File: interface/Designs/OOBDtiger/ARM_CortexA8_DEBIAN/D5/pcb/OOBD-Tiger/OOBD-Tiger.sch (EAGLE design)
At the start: 88 parts, among them IC3 DS1307, IC4 DS3231, Q2 32.768kHz, U1 SY6280, U10 MP1482DS, U2 SN65HVD230(SO8), U6 SN65HVD230(SO8)

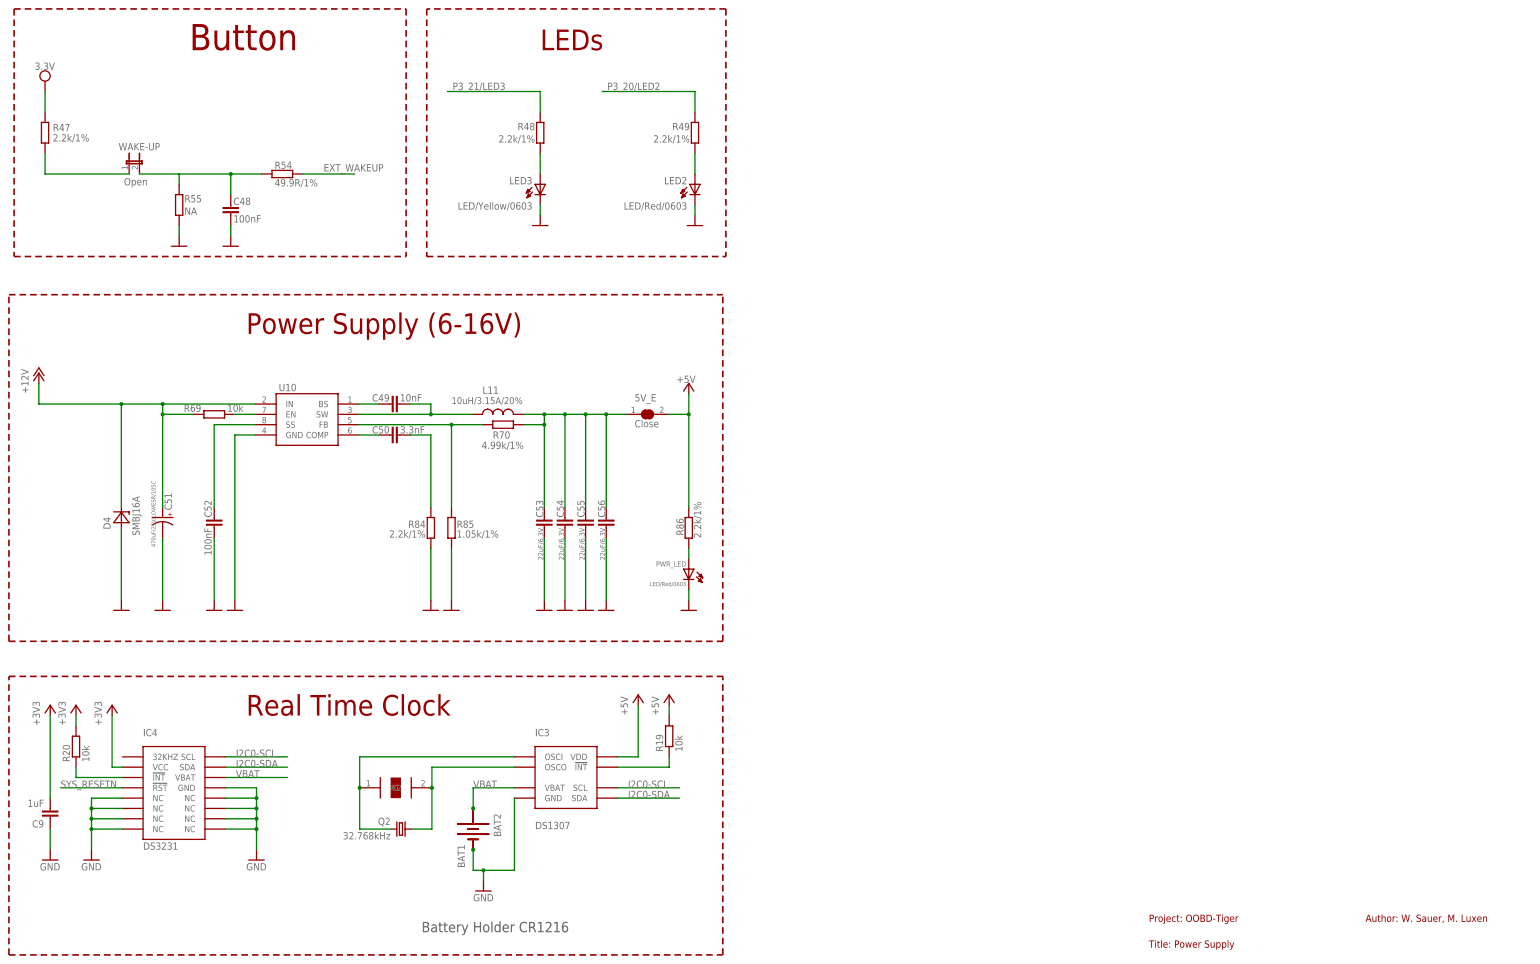
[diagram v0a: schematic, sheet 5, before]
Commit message: - delete further unneeded files(.lbr) - fix and rename Olimex_Connector.lbr to OOBDtiger-Connector.lbr - fix inconsistency error between schematic and pcb - create regular Projects for AM3352-SOM-EVB and OOBD-Tiger.brd - fix all ERC errors (only some uncritical warnings are open) - update OOBD-Tiger.pdf to visualize current status - fix TLV320AIC3107.lbr (=> but sym and dev is missing)
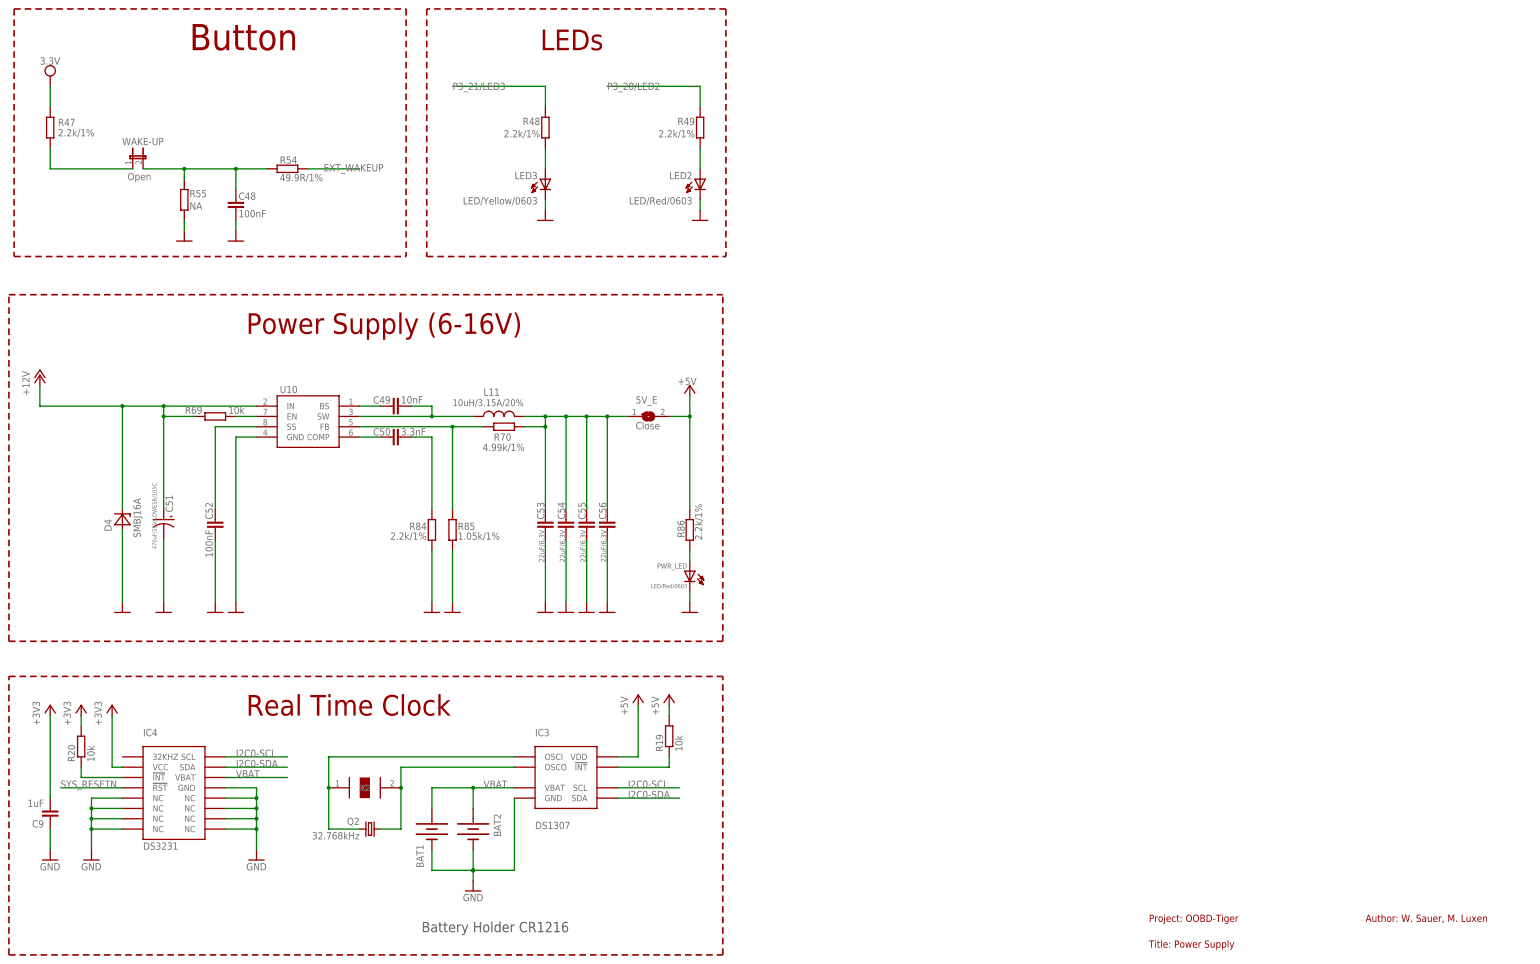
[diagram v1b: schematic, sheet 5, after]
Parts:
- AM3352-SOM-EVB-PLATFORM: device Tiger-connector_new:AM3352-SOM-EVB---4XGPH127SMT-02X20(PA-V16X-2X20-LF) -> OOBDtiger-Connector:OOBD-TIGER-AM3352-SOM---4XGPH127SMT-02X20(PA-V16X-2X20-LF)
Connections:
- removed net GNDA: AM3352-SOM-EVB-PLATFORM.GNDA
- removed net N$13: MS-CAN.2
- removed net N$30: L6.2
- new net N$10: MS-CAN.2, R42.1
- net GND: now also AM3352-SOM-EVB-PLATFORM.GNDA
- net N$29: now also L6.2
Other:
- moved on the sheet: 5V_E, BAT1, C10, C3, C48, C49, C50, C51, C52, C53, C54, C55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

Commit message: Aufgeräumt mit Mike
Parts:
- removed BAT1: (no value), SparkFun:BATTERY12MM
- removed IC3: DS1307, PierpaoloSmartSpaceSolutions:PCF8523SOIC8
- removed Q2: 32.768kHz, crystal:CRYSTALTC26H
- removed R19: 10k, rcl:R-EU_R0603
- removed U$3: XTAL32K, PierpaoloSmartSpaceSolutions:XTAL32K
- C1, C47: device rcl:C-EU025-024X044 -> rcl:C-EU2
- R7: device rcl:R-EU_0204/2V -> rcl:R-EU_R0603
- USB_HOST2: device OLIMEX_CONNECTORS:USB_SHIELDUSB_A_VERTICAL -> OLIMEX_CONNECTORS:USB_SHIELD1
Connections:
- removed net N$3: IC3.!INT, R19.1
- removed net OSCI: IC3.OSCI, Q2.2, U$3.X1
- removed net OSCO: IC3.OSCO, Q2.1, U$3.X2
- net +5V: no longer IC3.VDD, R19.2
- net GND: no longer BAT1.-, IC3.GND
- net I2C0-SCL: no longer IC3.SCL
- net I2C0-SDA: no longer IC3.SDA
- net VBAT: no longer BAT1.+, IC3.VBAT
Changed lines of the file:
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@@
 <?xml version="1.0" encoding="utf-8"?>
 <!DOCTYPE eagle SYSTEM "eagle.dtd">
-<eagle version="6.4">
+<eagle version="7.6.0">
 <drawing>
 <settings>
@@
 <part name="R41" library="rcl" deviceset="R-EU_" device="0204/2V" value="10k"/>
 <part name="V52" library="supply2" deviceset="VCC" device="" value="3.3V"/>
-<part name="C47" library="rcl" deviceset="C-EU" device="025-024X044" value="100nF"/>
+<part name="C47" library="rcl" deviceset="C-EU" device="2" value="100nF"/>
 <part name="GND98" library="supply1" deviceset="GND" device="" value=""/>
 <part name="R42" library="rcl" deviceset="R-EU_" device="0204/2V" value="120R"/>
@@
 <part name="R5" library="rcl" deviceset="R-EU_" device="0204/2V" value="10k"/>
 <part name="V2" library="supply2" deviceset="VCC" device="" value="3.3V"/>
-<part name="C1" library="rcl" deviceset="C-EU" device="025-024X044" value="100nF"/>
+<part name="C1" library="rcl" deviceset="C-EU" device="2" value="100nF"/>
 <part name="GND5" library="supply1" deviceset="GND" device="" value=""/>
 <part name="R6" library="rcl" deviceset="R-EU_" device="0204/2V" value="120R"/>
-<part name="R7" library="rcl" deviceset="R-EU_" device="0204/2V" value="NA"/>
+<part name="R7" library="rcl" deviceset="R-EU_" device="R0603" value="NA"/>
 <part name="OBD2-CONNECTOR" library="pinhead" deviceset="PINHD-2X5" device="/90"/>
 <part name="R8" library="resistor" deviceset="R-EU_" device="R0603" value="10K">
@@
 <part name="P+2" library="supply1" deviceset="+12V" device=""/>
 <part name="P+4" library="supply1" deviceset="+12V" device=""/>
-<part name="U$3" library="PierpaoloSmartSpaceSolutions" deviceset="XTAL32K" device=""/>
-<part name="Q2" library="crystal" deviceset="CRYSTAL" device="TC26H" value="32.768kHz"/>
 <part name="GND7" library="supply1" deviceset="GND" device=""/>
-<part name="IC3" library="PierpaoloSmartSpaceSolutions" deviceset="PCF8523" device="SOIC8" value="DS1307"/>
 <part name="GND33" library="supply1" deviceset="GND" device=""/>
 <part name="C9" library="rcl" deviceset="C-EU" device="C0603" value="1uF"/>
-<part name="R19" library="rcl" deviceset="R-EU_" device="R0603" value="10k"/>
-<part name="BAT1" library="SparkFun" deviceset="BATTERY" device="12MM"/>
-<part name="P+14" library="supply1" deviceset="+5V" device=""/>
 <part name="IC4" library="DS3231_industrialberry" deviceset="DS3231" device="SOIC-16W" value="DS3231"/>
 <part name="GND11" library="supply1" deviceset="GND" device=""/>
 <part name="GND16" library="supply1" deviceset="GND" device=""/>
 <part name="BAT2" library="SparkFun" deviceset="BATTERY" device="12PTH"/>
-<part name="USB_HOST2" library="OLIMEX_CONNECTORS" deviceset="USB_SHIELD" device="USB_A_VERTICAL" value="USB_A_VERTICAL"/>
+<part name="USB_HOST2" library="OLIMEX_CONNECTORS" deviceset="USB_SHIELD" device="1" value="USB_A_VERTICAL"/>
 <part name="L5" library="rcl" deviceset="L-US" device="L0805_5MIL_DWS" value="FB0805/600R/2A"/>
 <part name="C3" library="rcl" deviceset="C-EU" device="C0603_DWS" value="100nF"/>
@@
 <part name="+3V2" library="supply1" deviceset="+3V3" device=""/>
 <part name="R20" library="rcl" deviceset="R-EU_" device="R0603" value="10k"/>
-<part name="P+6" library="supply1" deviceset="+5V" device=""/>
 <part name="+3V3" library="supply1" deviceset="+3V3" device=""/>
 <part name="+3V4" library="supply1" deviceset="+3V3" device=""/>
@@
 <instance part="GND26" gate="1" x="157.48" y="96.52"/>
 <instance part="P+4" gate="1" x="17.78" y="154.94"/>
-<instance part="U$3" gate="G$1" x="96.52" y="53.34" rot="MR180"/>
-<instance part="Q2" gate="G$1" x="99.06" y="43.18" rot="MR0"/>
 <instance part="GND7" gate="1" x="124.46" y="27.94"/>
-<instance part="IC3" gate="G$1" x="147.32" y="55.88"/>
 <instance part="GND33" gate="1" x="20.32" y="35.56"/>
 <instance part="C9" gate="G$1" x="20.32" y="45.72" rot="R180"/>
-<instance part="R19" gate="G$1" x="172.72" y="66.04" rot="R90"/>
-<instance part="BAT1" gate="G$1" x="114.3" y="43.18" smashed="yes" rot="R270">
-<attribute name="NAME" x="110.49" y="39.37" size="1.778" layer="95" rot="R270"/>
-<attribute name="VALUE" x="107.95" y="46.99" size="1.778" layer="96" rot="R270"/>
-</instance>
-<instance part="P+14" gate="1" x="165.1" y="76.2"/>
 <instance part="IC4" gate="G$1" x="50.8" y="50.8"/>
 <instance part="GND11" gate="1" x="71.12" y="35.56"/>
@@
 <instance part="+3V2" gate="G$1" x="35.56" y="73.66"/>
 <instance part="R20" gate="G$1" x="27.94" y="63.5" rot="R90"/>
-<instance part="P+6" gate="1" x="172.72" y="76.2"/>
 <instance part="+3V3" gate="G$1" x="27.94" y="73.66"/>
 </instances>
@@
 </segment>
 <segment>
-<wire x1="124.46" y1="33.02" x2="124.46" y2="30.48" width="0.1524" layer="91"/>
-<wire x1="124.46" y1="33.02" x2="134.62" y2="33.02" width="0.1524" layer="91"/>
-<wire x1="134.62" y1="33.02" x2="134.62" y2="50.8" width="0.1524" layer="91"/>
-<junction x="124.46" y="33.02"/>
 <pinref part="GND7" gate="1" pin="GND"/>
-<pinref part="IC3" gate="G$1" pin="GND"/>
-<pinref part="BAT1" gate="G$1" pin="-"/>
 <pinref part="BAT2" gate="G$1" pin="-"/>
-<wire x1="124.46" y1="38.1" x2="124.46" y2="33.02" width="0.1524" layer="91"/>
-<wire x1="124.46" y1="33.02" x2="114.3" y2="33.02" width="0.1524" layer="91"/>
-<wire x1="114.3" y1="33.02" x2="114.3" y2="38.1" width="0.1524" layer="91"/>
-<junction x="124.46" y="33.02"/>
+<wire x1="124.46" y1="38.1" x2="124.46" y2="30.48" width="0.1524" layer="91"/>
 </segment>
 <segment>
@@
 <pinref part="P+5" gate="1" pin="+5V"/>
 <pinref part="R86" gate="G$1" pin="1"/>
-</segment>
-<segment>
-<wire x1="165.1" y1="60.96" x2="165.1" y2="73.66" width="0.1524" layer="91"/>
-<wire x1="160.02" y1="60.96" x2="165.1" y2="60.96" width="0.1524" layer="91"/>
-<pinref part="IC3" gate="G$1" pin="VDD"/>
-<pinref part="P+14" gate="1" pin="+5V"/>
-</segment>
-<segment>
-<wire x1="172.72" y1="73.66" x2="172.72" y2="71.12" width="0.1524" layer="91"/>
-<pinref part="R19" gate="G$1" pin="2"/>
-<pinref part="P+6" gate="1" pin="+5V"/>
 </segment>
 </net>
@@
 <net name="I2C0-SDA" class="0">
 <segment>
-<wire x1="175.26" y1="50.8" x2="160.02" y2="50.8" width="0.1524" layer="91"/>
-<label x="162.56" y="50.8" size="1.778" layer="95"/>
-<pinref part="IC3" gate="G$1" pin="SDA"/>
-</segment>
-<segment>
 <wire x1="78.74" y1="58.42" x2="63.5" y2="58.42" width="0.1524" layer="91"/>
 <label x="66.04" y="58.42" size="1.778" layer="95"/>
@@
 <net name="I2C0-SCL" class="0">
 <segment>
-<wire x1="175.26" y1="53.34" x2="160.02" y2="53.34" width="0.1524" layer="91"/>
-<label x="162.56" y="53.34" size="1.778" layer="95"/>
-<pinref part="IC3" gate="G$1" pin="SCL"/>
-</segment>
-<segment>
 <wire x1="78.74" y1="60.96" x2="63.5" y2="60.96" width="0.1524" layer="91"/>
 <label x="66.04" y="60.96" size="1.778" layer="95"/>
@@
 </segment>
 </net>
-<net name="N$3" class="0">
-<segment>
-<wire x1="160.02" y1="58.42" x2="172.72" y2="58.42" width="0.1524" layer="91"/>
-<wire x1="172.72" y1="58.42" x2="172.72" y2="60.96" width="0.1524" layer="91"/>
-<pinref part="IC3" gate="G$1" pin="!INT"/>
-<pinref part="R19" gate="G$1" pin="1"/>
-</segment>
-</net>
 <net name="VBAT" class="0">
 <segment>
@@
 </segment>
 <segment>
-<pinref part="BAT1" gate="G$1" pin="+"/>
-<wire x1="114.3" y1="48.26" x2="114.3" y2="53.34" width="0.1524" layer="91"/>
-<pinref part="IC3" gate="G$1" pin="VBAT"/>
-<wire x1="114.3" y1="53.34" x2="124.46" y2="53.34" width="0.1524" layer="91"/>
 <pinref part="BAT2" gate="G$1" pin="+"/>
-<wire x1="124.46" y1="53.34" x2="134.62" y2="53.34" width="0.1524" layer="91"/>
 <wire x1="124.46" y1="48.26" x2="124.46" y2="53.34" width="0.1524" layer="91"/>
-<junction x="124.46" y="53.34"/>
 <label x="127" y="53.34" size="1.778" layer="95"/>
 </segment>
 </net>
-<net name="OSCI" class="0">
-<segment>
-<wire x1="96.52" y1="43.18" x2="88.9" y2="43.18" width="0.1524" layer="91"/>
-<wire x1="88.9" y1="43.18" x2="88.9" y2="53.34" width="0.1524" layer="91"/>
-<wire x1="88.9" y1="53.34" x2="88.9" y2="60.96" width="0.1524" layer="91"/>
-<junction x="88.9" y="53.34"/>
-<pinref part="Q2" gate="G$1" pin="2"/>
-<pinref part="U$3" gate="G$1" pin="X1"/>
-<wire x1="88.9" y1="60.96" x2="134.62" y2="60.96" width="0.1524" layer="91"/>
-<pinref part="IC3" gate="G$1" pin="OSCI"/>
-</segment>
-</net>
-<net name="OSCO" class="0">
-<segment>
-<wire x1="101.6" y1="43.18" x2="106.68" y2="43.18" width="0.1524" layer="91"/>
-<wire x1="106.68" y1="43.18" x2="106.68" y2="53.34" width="0.1524" layer="91"/>
-<wire x1="106.68" y1="53.34" x2="106.68" y2="58.42" width="0.1524" layer="91"/>
-<junction x="106.68" y="53.34"/>
-<pinref part="Q2" gate="G$1" pin="1"/>
-<pinref part="U$3" gate="G$1" pin="X2"/>
-<pinref part="IC3" gate="G$1" pin="OSCO"/>
-<wire x1="134.62" y1="58.42" x2="106.68" y2="58.42" width="0.1524" layer="91"/>
-</segment>
-</net>

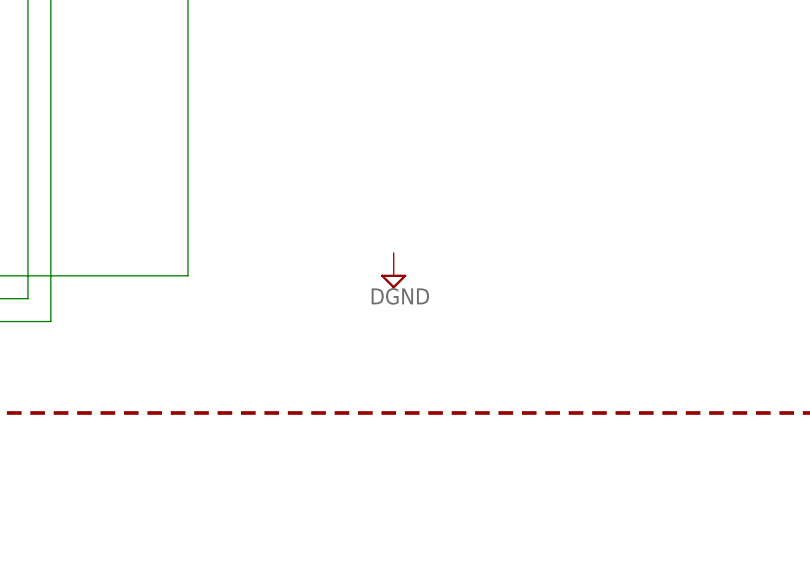
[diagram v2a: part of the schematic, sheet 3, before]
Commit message: Erster Schritt vereinheitlichen der Packabes, finetuning bzgl. Positionen, Validierung einzelner Signalnamen fortgeschritten aber noch nicht abgeschlossen. Versuchsweise geroutet um ein Gefühl dafür zu bekommen wo Bottlenecks sind
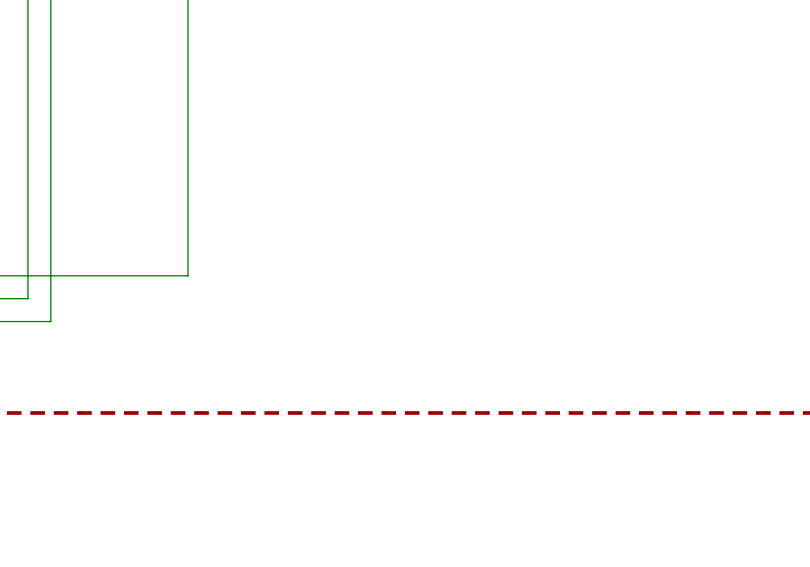
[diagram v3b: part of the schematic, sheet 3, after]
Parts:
- C16, C17, C18, C19, C5, C7: device SparkFun-Passives:CAP0402-CAP -> SparkFun-Passives:CAP0603-CAP
- C4, C48, C49, C50, C52, C53, C54, C55, C56, C6, C63, C64: device rcl:C-EU025-024X044 -> rcl:C-EUC0603
- L1, L3: device rcl:L-US0204/5 -> rcl:L-USL0603
- R1, R2, R3, R4, R40, R41, R42, R47, R48, R49, R5, R54, R55, R6, R69, R70, R84, R85, R86: device rcl:R-EU_0204/2V -> rcl:R-EU_R0603
